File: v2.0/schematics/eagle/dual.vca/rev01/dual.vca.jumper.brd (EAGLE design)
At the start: 89.8 x 27.9 mm, 3 parts

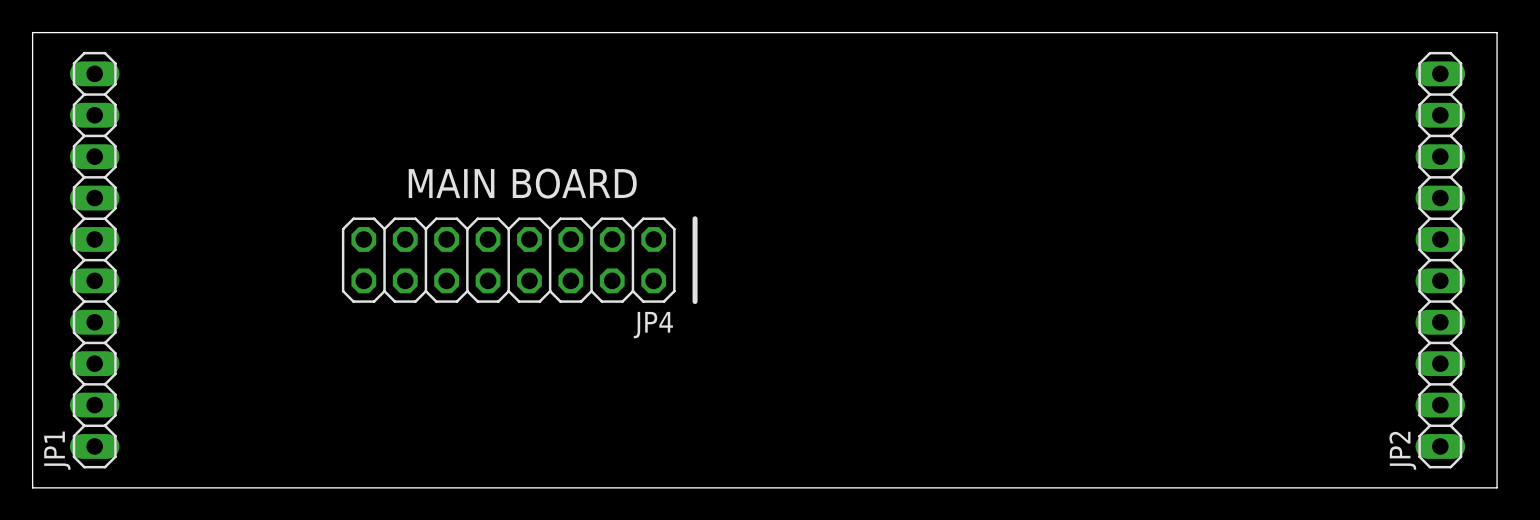
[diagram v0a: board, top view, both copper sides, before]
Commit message: Dual VCA jumper board ground planes and autoroute
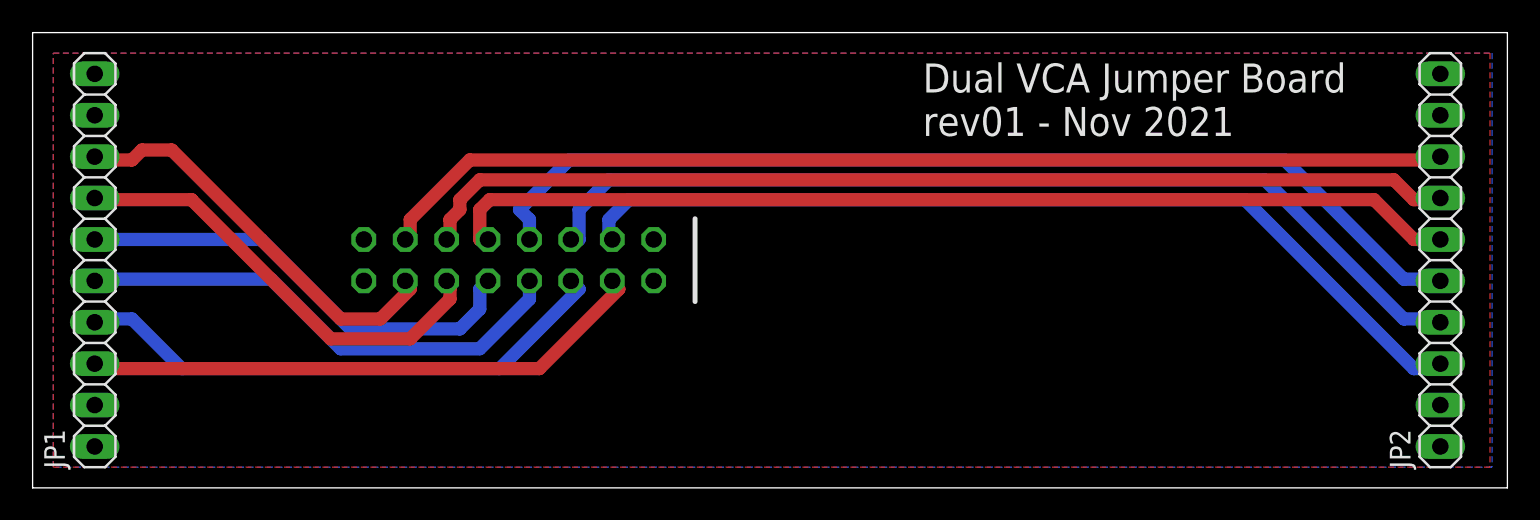
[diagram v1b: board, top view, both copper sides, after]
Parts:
- JP4: value (none) -> TO MAIN
- flipped JP4 to the bottom, turned to 0 degrees
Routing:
- net OUT4: track 0.00 -> 66.3 mm
- net IN4: track 0.00 -> 64.1 mm
- net CV3: track 0.00 -> 62.9 mm
- net CV4: track 0.00 -> 62.5 mm
- net OUT3: track 0.00 -> 59.5 mm
- net IN3: track 0.00 -> 57.3 mm
- net IN1: track 0.00 -> 34.9 mm
- net OUT1: track 0.00 -> 33.8 mm
- net CV1: track 0.00 -> 30.8 mm
- net CV2: track 0.00 -> 28.3 mm
- net IN2: track 0.00 -> 27.5 mm
- net OUT2: track 0.00 -> 25.3 mm
- added copper zone on layer 1, net 0V
- added copper zone on layer 16, net 0V
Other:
- board size 89.8 x 27.9 mm -> 90.5 x 27.9 mm
- board text added: "Dual VCA Jumper Board rev01 - Nov 2021"
